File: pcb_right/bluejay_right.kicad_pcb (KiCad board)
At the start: 2 copper layers, 147 x 140.5 mm, 61 parts, among them J2 SJ-43514, U2 MCP23017

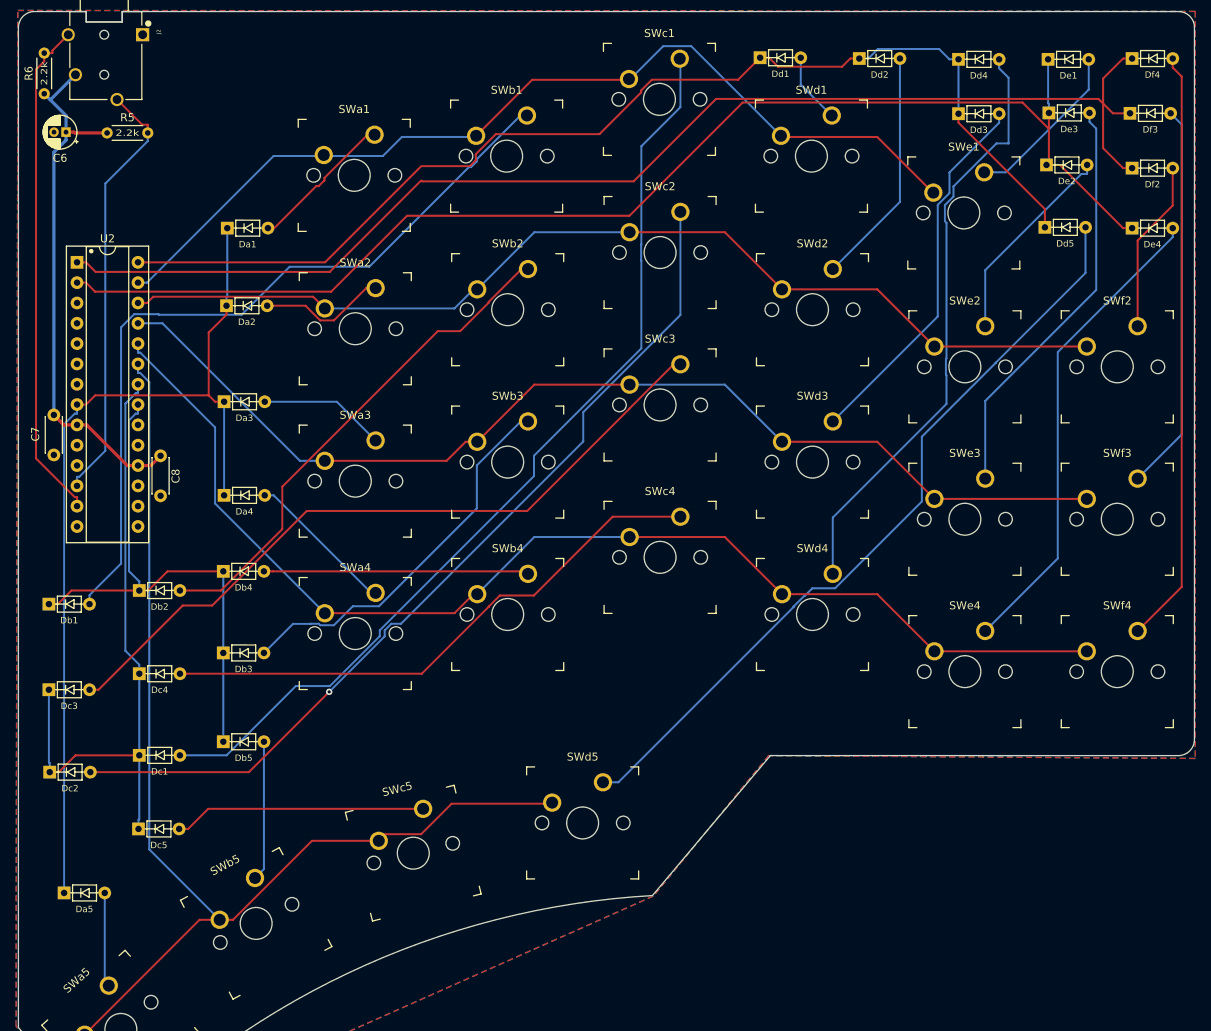
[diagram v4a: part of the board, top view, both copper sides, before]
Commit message: Fine tune alignment of diodes and resistors
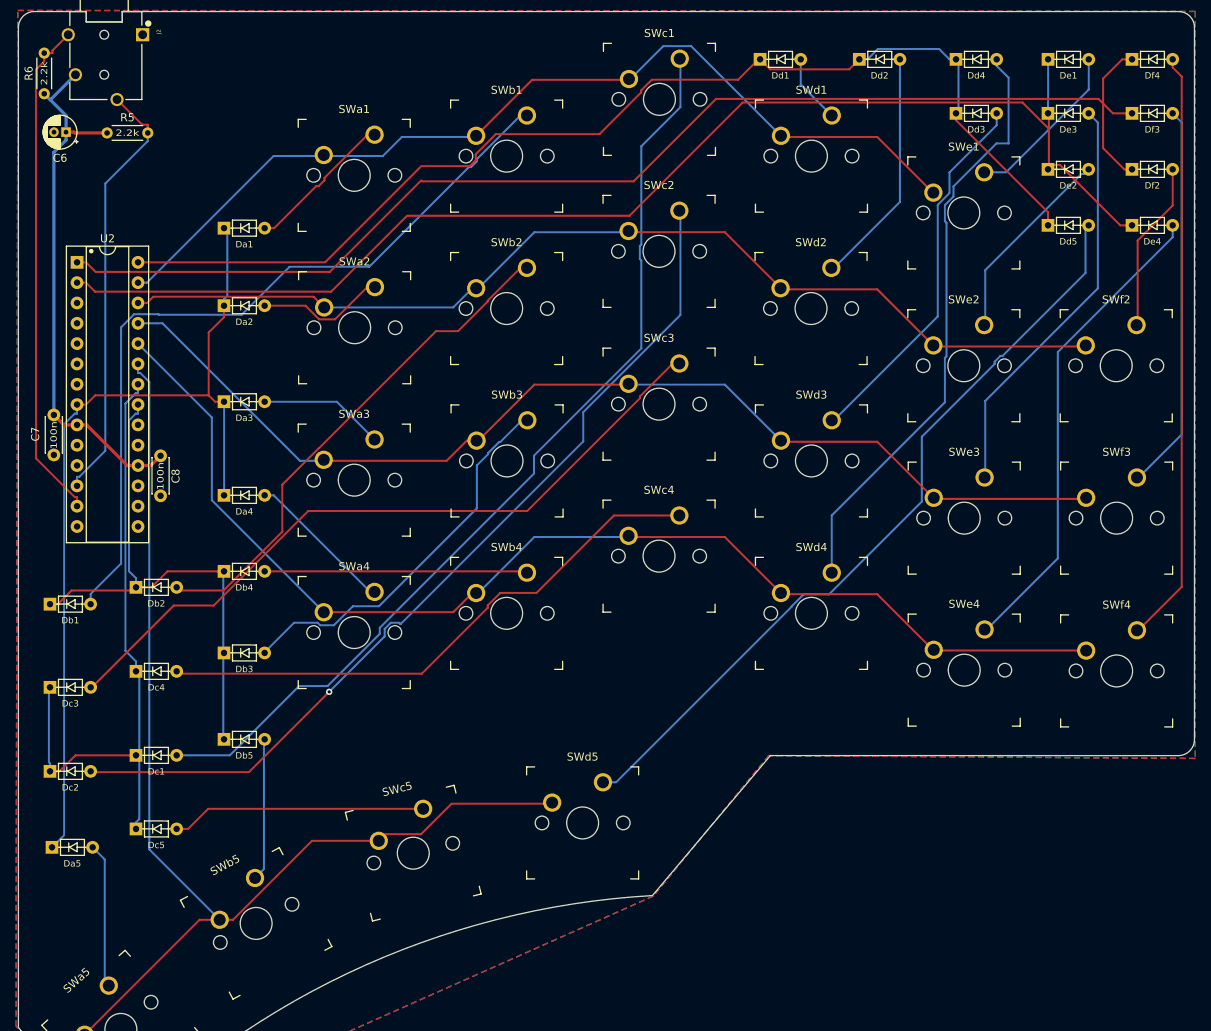
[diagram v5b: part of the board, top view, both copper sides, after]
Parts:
- moved Da5 5.90 mm to (77.5, 131.5)
- moved De2 0.58 mm to (202.0, 46.8)
- moved Db2 0.57 mm to (88.0, 99.0)
- moved Dc4 0.51 mm to (88.0, 109.5)
- moved Dd5 0.46 mm to (202.0, 53.8)
- moved Da1 0.41 mm to (99.0, 54.1)
- moved Dc1 0.41 mm to (88.0, 120.0)
- moved De4 0.35 mm to (212.5, 53.8)
- moved Dc3 0.33 mm to (77.2, 111.5)
- moved Dd3 0.32 mm to (190.5, 39.8)
- moved Da2 0.31 mm to (99.0, 63.8)
- moved Dc5 0.31 mm to (88.0, 129.2)
- moved Dd4 0.31 mm to (190.5, 33.0)
- moved Db5 0.31 mm to (99.0, 118.0)
- moved Df3 0.25 mm to (212.5, 39.8)
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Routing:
- net Net-(Da5-Pad2): track 11.8 -> 18.1 mm
- net /colA: track 114.6 -> 109.7 mm
- net Net-(Db2-Pad2): track 63.3 -> 64.2 mm
- net Net-(De2-Pad2): track 25.8 -> 25.1 mm
- net /colB: track 69.2 -> 68.4 mm
- net Net-(Dc4-Pad2): track 70.7 -> 71.3 mm
- net Net-(Dd5-Pad2): track 97.2 -> 97.7 mm

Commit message: No need for decoupling cap on reset pin
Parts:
- removed C8: 100n, BlueJay footprints:C_Disc_D4.3mm_W1.9mm_P5.00mm
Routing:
- net VCC: track 68.0 -> 64.7 mm
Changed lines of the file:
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@@
-    )
-  )
-  (footprint "BlueJay footprints:C_Disc_D4.3mm_W1.9mm_P5.00mm" (layer "F.Cu")
-    (at 92.34 82.56 -90)
-    (descr "C, Disc series, Radial, pin pitch=5.00mm, , diameter*width=4.3*1.9mm^2, Capacitor, http://www.vishay.com/docs/45233/krseries.pdf")
-    (tags "C Disc series Radial pin pitch 5.00mm  diameter 4.3mm width 1.9mm Capacitor")
-    (property "Sheetfile" "bluejay_right.kicad_sch")
-    (property "Sheetname" "")
-    (attr through_hole)
-    (fp_text reference "C8" (at 2.54 -1.905 90) (layer "F.SilkS")
-      (effects (font (size 1 1) (thickness 0.15)))
-    )
-    (fp_text value "100n" (at 2.54 0 90) (layer "F.SilkS")
-      (effects (font (size 0.8 1) (thickness 0.15)))
-    )
-    (fp_text user "${REFERENCE}" (at 2.5 0 90) (layer "F.Fab")
-      (effects (font (size 0.86 0.86) (thickness 0.129)))
-    )
-    (fp_line (start 4.77 1.055) (end 4.77 1.07) (layer "F.SilkS") (width 0.12))
-    (fp_line (start 0.23 -1.07) (end 0.23 -1.055) (layer "F.SilkS") (width 0.12))
-    (fp_line (start 0.23 1.07) (end 4.77 1.07) (layer "F.SilkS") (width 0.12))
-    (fp_line (start 0.23 1.055) (end 0.23 1.07) (layer "F.SilkS") (width 0.12))
-    (fp_line (start 0.23 -1.07) (end 4.77 -1.07) (layer "F.SilkS") (width 0.12))
-    (fp_line (start 4.77 -1.07) (end 4.77 -1.055) (layer "F.SilkS") (width 0.12))
-    (fp_line (start -1.05 -1.2) (end -1.05 1.2) (layer "F.CrtYd") (width 0.05))
-    (fp_line (start 6.05 1.2) (end 6.05 -1.2) (layer "F.CrtYd") (width 0.05))
-    (fp_line (start 6.05 -1.2) (end -1.05 -1.2) (layer "F.CrtYd") (width 0.05))
-    (fp_line (start -1.05 1.2) (end 6.05 1.2) (layer "F.CrtYd") (width 0.05))
-    (fp_line (start 4.65 -0.95) (end 0.35 -0.95) (layer "F.Fab") (width 0.1))
-    (fp_line (start 0.35 0.95) (end 4.65 0.95) (layer "F.Fab") (width 0.1))
-    (fp_line (start 0.35 -0.95) (end 0.35 0.95) (layer "F.Fab") (width 0.1))
-    (fp_line (start 4.65 0.95) (end 4.65 -0.95) (layer "F.Fab") (width 0.1))
-    (pad "1" thru_hole circle (at 0 0 270) (size 1.6 1.6) (drill 0.8) (layers *.Cu *.Mask)
-      (net 1 "VCC") (pintype "passive"))
-    (pad "2" thru_hole circle (at 5 0 270) (size 1.6 1.6) (drill 0.8) (layers *.Cu *.Mask)
-      (net 2 "GND") (pintype "passive"))
-    (model "${KICAD6_3DMODEL_DIR}/Capacitor_THT.3dshapes/C_Disc_D4.3mm_W1.9mm_P5.00mm.wrl"
-      (offset (xyz 0 0 0))
-      (scale (xyz 1 1 1))
-      (rotate (xyz 0 0 0))
     )
   )
@@
   (gr_line (start 74.572157 29.03) (end 74.572156 154.03) (layer "Edge.Cuts") (width 0.1))
   (gr_arc (start 219.577845 27.03) (mid 220.996071 27.606272) (end 221.577845 29.02225) (layer "Edge.Cuts") (width 0.1))
-  (segment (start 89.52 83.775) (end 91.125 83.775) (width 0.4) (layer "F.Cu") (net 1))
   (segment (start 80.5226 42.1) (end 81.5229 42.1) (width 0.4) (layer "F.Cu") (net 1))
   (segment (start 85.66 42.2) (end 81.6229 42.2) (width 0.4) (layer "F.Cu") (net 1))
-  (segment (start 91.125 83.775) (end 92.34 82.56) (width 0.4) (layer "F.Cu") (net 1))
   (segment (start 80.245 78.695) (end 81.9 78.695) (width 0.4) (layer "F.Cu") (net 1))
   (segment (start 83.1003 78.695) (end 88.1803 83.775) (width 0.4) (layer "F.Cu") (net 1))

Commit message: Add mounting holes
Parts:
- added H1: M2, MountingHole:MountingHole_2.2mm_M2_Pad, F.Cu at (82.2, -52.6)
- added H2: M2, MountingHole:MountingHole_2.2mm_M2_Pad, F.Cu at (-57.2, -52.5)
- added H3: M2, MountingHole:MountingHole_2.2mm_M2_Pad, F.Cu at (-9.40, -27.6)
- added H4: M2, MountingHole:MountingHole_2.2mm_M2_Pad, F.Cu at (66.8, -2.40)
- added H5: M2, MountingHole:MountingHole_2.2mm_M2_Pad, F.Cu at (28.6, 9.50)
- added H6: M2, MountingHole:MountingHole_2.2mm_M2_Pad, F.Cu at (66.8, 16.6)
- added H7: M2, MountingHole:MountingHole_2.2mm_M2_Pad, F.Cu at (-1.60, 46.0)
- added H8: M2, MountingHole:MountingHole_2.2mm_M2_Pad, F.Cu at (-40.9, 63.3)
- added H9: M2, MountingHole:MountingHole_2.2mm_M2_Pad, F.Cu at (-57.2, 66.4)
- moved C7 159.1 mm to (-56.6, -5.75)
- moved Da1 159.1 mm to (-36.6, -29.1)
- moved Da2 159.1 mm to (-36.6, -19.4)
- moved Da3 159.1 mm to (-36.6, -7.40)
- moved Da4 159.1 mm to (-36.6, 4.30)
- moved Da5 159.1 mm to (-58.1, 48.3)
- moved Db1 159.1 mm to (-58.4, 17.9)
- moved Db2 159.1 mm to (-47.6, 15.8)
- moved Db3 159.1 mm to (-36.6, 24.0)
- moved Db4 159.1 mm to (-36.6, 13.8)
- moved Db5 159.1 mm to (-36.6, 34.8)
- moved Dc1 159.1 mm to (-47.6, 36.8)
- moved Dc2 159.1 mm to (-58.4, 38.8)
- moved Dc3 159.1 mm to (-58.4, 28.3)
- moved Dc4 159.1 mm to (-47.6, 26.3)
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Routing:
- net VCC: track 64.7 -> 66.7 mm
- net Net-(Df4-Pad2): track 74.3 -> 73.0 mm
- net /i2c_SDA: track 63.5 -> 64.6 mm
- net /colF: track 160.0 -> 159.3 mm
- net /i2c_SCL: track 54.1 -> 53.6 mm
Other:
- outline, holes or cut-outs redrawn

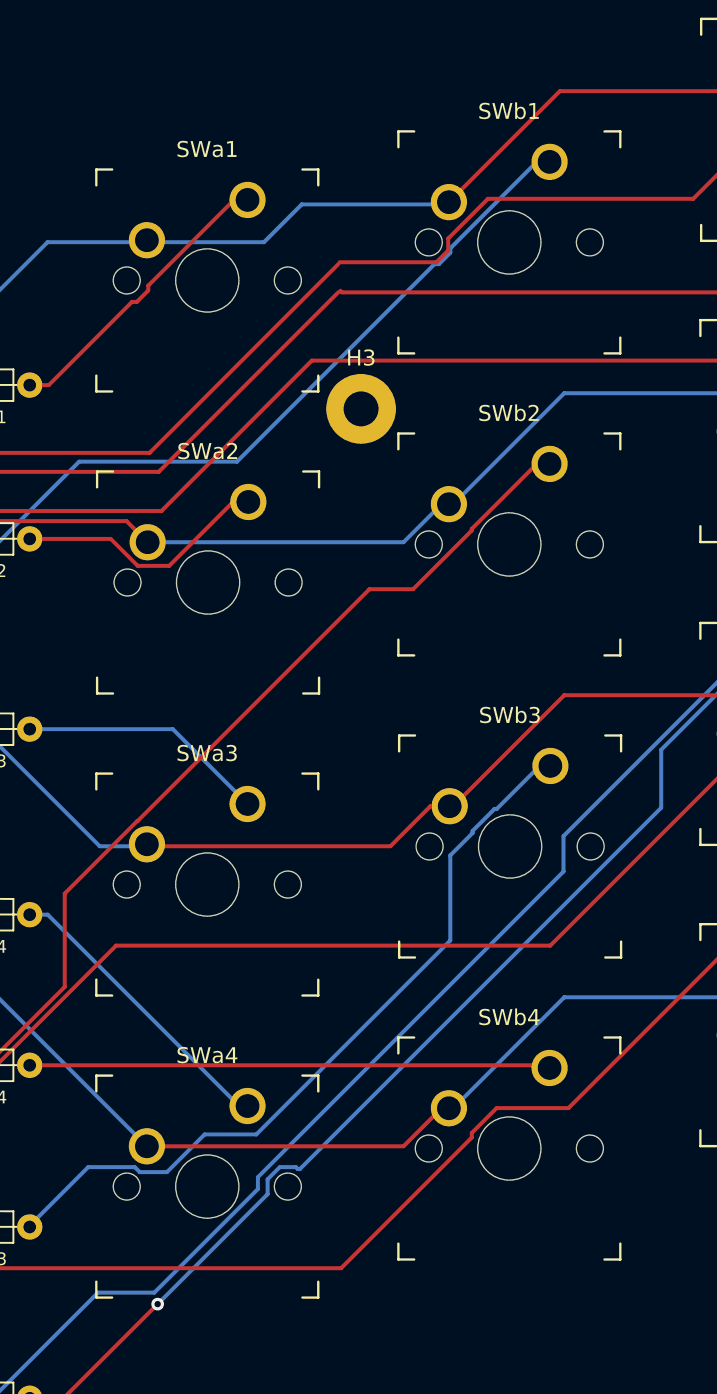
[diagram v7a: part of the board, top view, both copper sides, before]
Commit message: Tweak placement of components on left hand
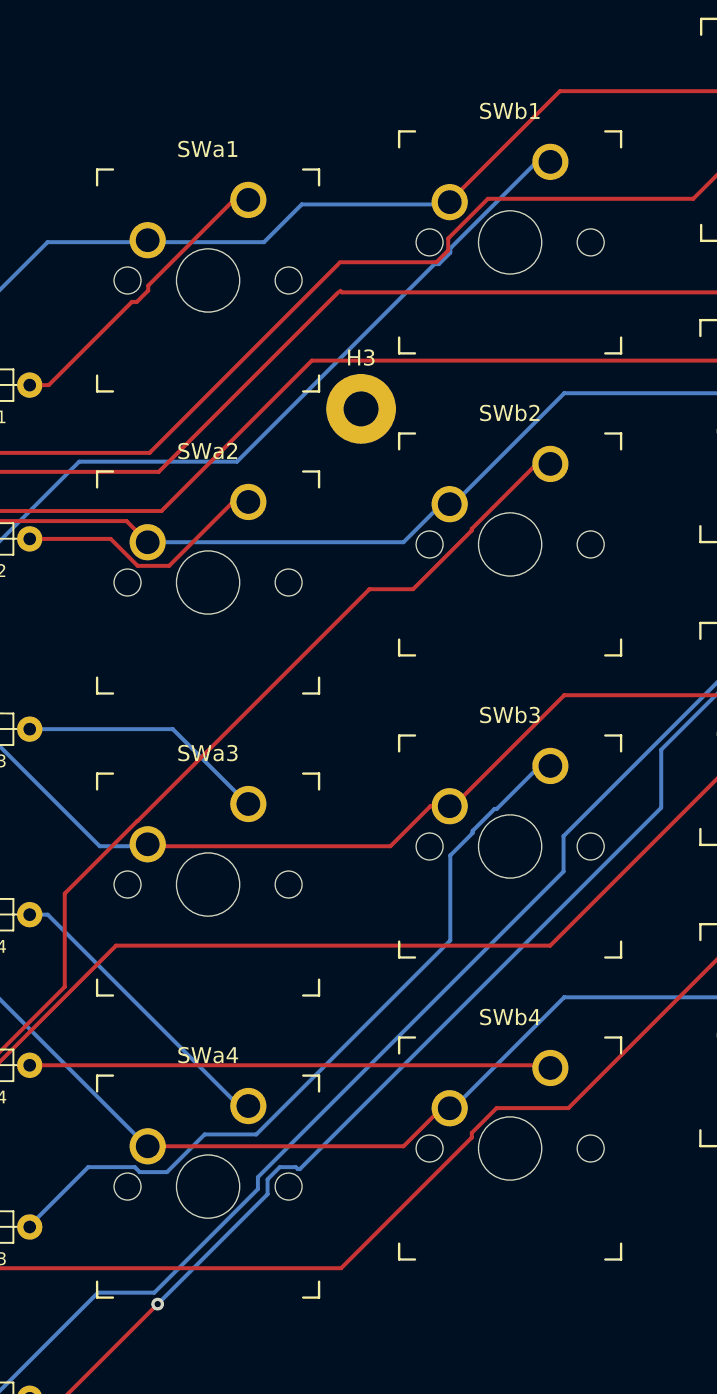
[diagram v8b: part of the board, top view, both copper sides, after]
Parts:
- moved SWa1 0.05 mm to (-19.1, -35.7)
- moved SWa3 0.05 mm to (-19.1, 2.40)
- moved SWa4 0.05 mm to (-19.1, 21.4)
- moved SWb1 0.05 mm to (0.00, -38.1)
- moved SWb2 0.05 mm to (0.00, -19.1)
- moved SWb4 0.05 mm to (0.00, 19.1)
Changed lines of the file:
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@@
   )
   (footprint "BlueJay footprints:SW_MX" (layer "F.Cu")
-    (at -0.05 -38.1)
+    (at 0 -38.1)
     (descr "MX-style keyswitch")
     (tags "MX,cherry,gateron,kailh")
@@
   )
   (footprint "BlueJay footprints:SW_MX" (layer "F.Cu")
-    (at -19.1 2.4)
+    (at -19.05 2.4)
     (descr "MX-style keyswitch")
     (tags "MX,cherry,gateron,kailh")
@@
   )
   (footprint "BlueJay footprints:SW_MX" (layer "F.Cu")
-    (at -0.05 -19.05)
+    (at 0 -19.05)
     (descr "MX-style keyswitch")
     (tags "MX,cherry,gateron,kailh")
@@
   )
   (footprint "BlueJay footprints:SW_MX" (layer "F.Cu")
-    (at -0.05 19.05)
+    (at 0 19.05)
     (descr "MX-style keyswitch")
     (tags "MX,cherry,gateron,kailh")
@@
   )
   (footprint "BlueJay footprints:SW_MX" (layer "F.Cu")
-    (at -19.1 -35.7)
+    (at -19.05 -35.7)
     (descr "MX-style keyswitch")
     (tags "MX,cherry,gateron,kailh")
@@
   )
   (footprint "BlueJay footprints:SW_MX" (layer "F.Cu")
-    (at -19.1 21.45)
-    (descr "MX-style keyswitch")
-    (tags "MX,cherry,gateron,kailh")
+    (at -19.05 21.45)
+    (descr "MX-style keyswitch")
+    (tags "MX,cherry,gateron,kailh")
